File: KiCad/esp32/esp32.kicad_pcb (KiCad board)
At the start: 2 copper layers, 2 parts, among them U1 ESD7104MUTAG, U2 ESP32-S3-MINI-1-N8

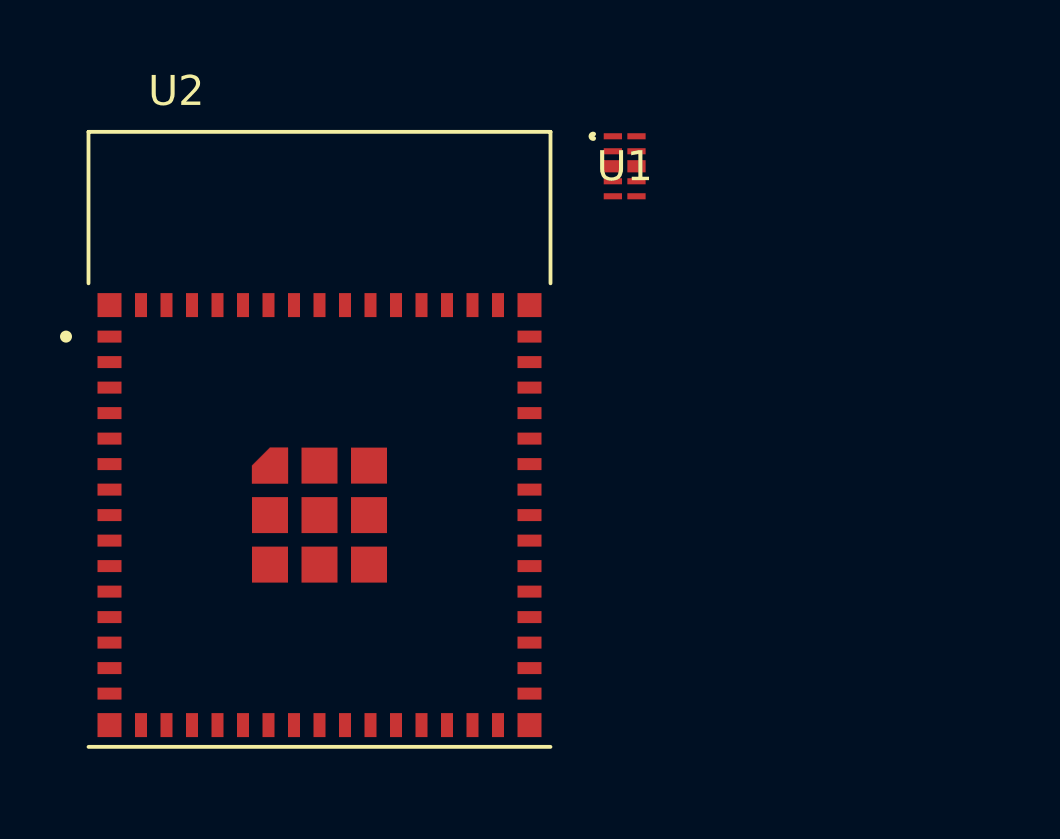
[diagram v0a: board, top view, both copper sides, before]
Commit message: restructed the path and file strcter
upaded schiemate and update pcb layout
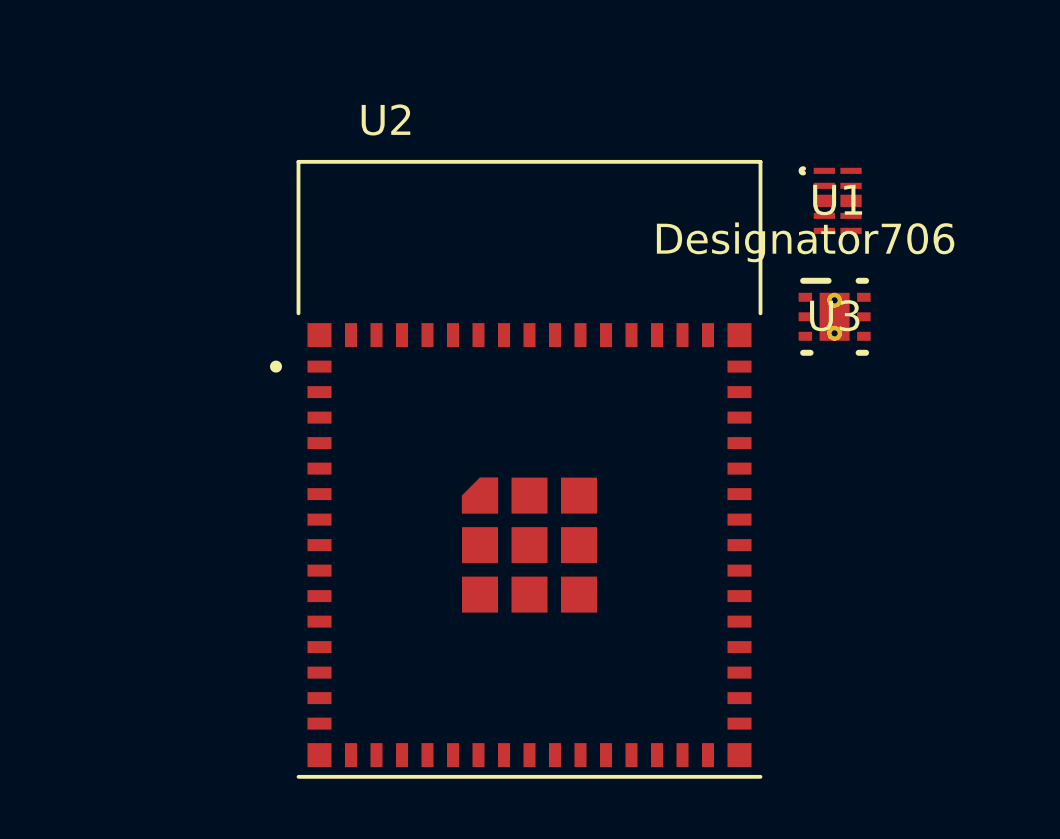
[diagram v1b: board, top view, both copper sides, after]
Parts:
- added U3: TLV75801PDRVR, Footprint:DRV0006A, F.Cu at (85.7, 92.4)
- U1: footprint footprints:UDFN10_ONS-L -> Footprint:UDFN10_ONS
- U2: footprint ESP32_S3_MINI_1_N8:XCVR_ESP32-S3-MINI-1-N8 -> Footprint:XCVR_ESP32-S3-MINI-1-N8
- moved U1 7.19 mm to (85.8, 88.5)
- moved U2 7.07 mm to (75.5, 100.0)

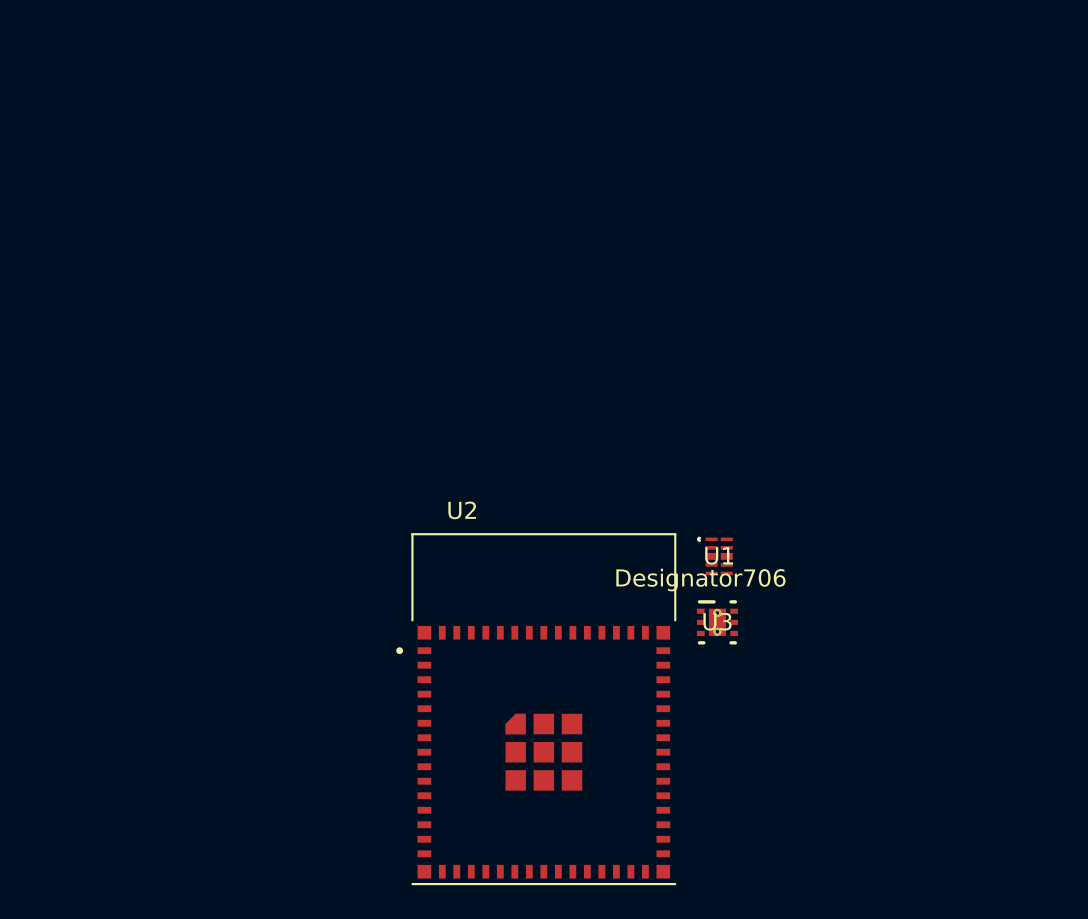
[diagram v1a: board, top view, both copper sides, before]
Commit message: layout started, footprints imported
pushed pcb
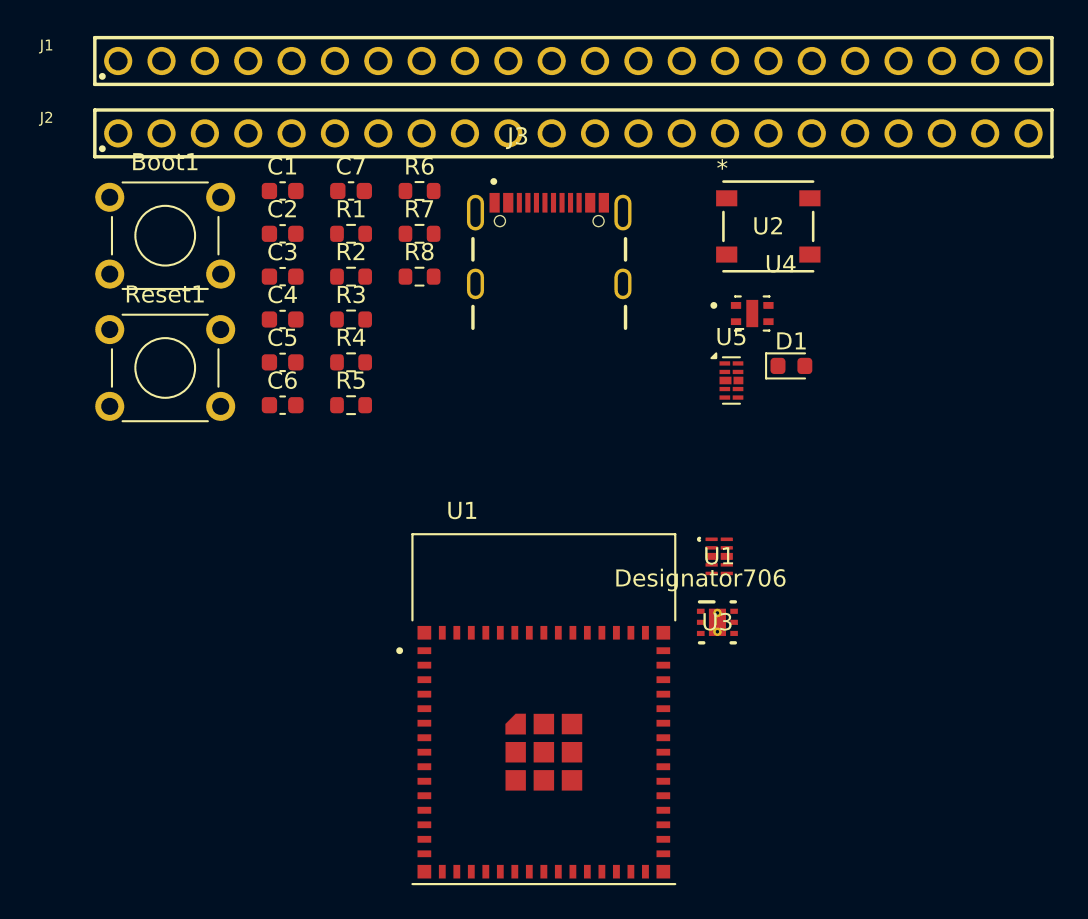
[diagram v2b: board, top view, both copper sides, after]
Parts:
- added Boot1: SW_Push_Dual, Button_Switch_THT:SW_TH_Tactile_Omron_B3F-100x, F.Cu at (50.1, 67.5)
- added C1: 0.1u, Capacitor_SMD:C_0603_1608Metric, F.Cu at (60.2, 67.1)
- added C2: 0.1u, Capacitor_SMD:C_0603_1608Metric, F.Cu at (60.2, 69.6)
- added C3: 0.1u, Capacitor_SMD:C_0603_1608Metric, F.Cu at (60.2, 72.1)
- added C4: 10u, Capacitor_SMD:C_0603_1608Metric, F.Cu at (60.2, 74.6)
- added C5: 10u, Capacitor_SMD:C_0603_1608Metric, F.Cu at (60.2, 77.2)
- added C6: 10u, Capacitor_SMD:C_0603_1608Metric, F.Cu at (60.2, 79.7)
- added C7: 0.1u, Capacitor_SMD:C_0603_1608Metric, F.Cu at (64.2, 67.1)
- added D1: LED, LED_SMD:LED_0603_1608Metric, F.Cu at (90.0, 77.4)
- added J1: 6130XX11121_61302211121, Footprint:61302211121, F.Cu at (77.2, 59.5)
- added J2: 6130XX11121_61302211121, Footprint:61302211121, F.Cu at (77.2, 63.7)
- added J3: USB4105-GF-A, Footprint:GCT_USB4105-GF-A, F.Cu at (75.8, 72.6)
- added R1: 10k, Resistor_SMD:R_0603_1608Metric, F.Cu at (64.2, 69.6)
- added R2: 10k, Resistor_SMD:R_0603_1608Metric, F.Cu at (64.2, 72.1)
- added R3: 10k, Resistor_SMD:R_0603_1608Metric, F.Cu at (64.2, 74.6)
- added R4: 5.1k, Resistor_SMD:R_0603_1608Metric, F.Cu at (64.2, 77.2)
- added R5: 5.1k, Resistor_SMD:R_0603_1608Metric, F.Cu at (64.2, 79.7)
- added R6: 1M, Resistor_SMD:R_0603_1608Metric, F.Cu at (68.2, 67.1)
- added R7: 200k, Resistor_SMD:R_0603_1608Metric, F.Cu at (68.2, 69.6)
- added R8: 5.1k, Resistor_SMD:R_0603_1608Metric, F.Cu at (68.2, 72.1)
- added Reset1: SW_Push_Dual, Button_Switch_THT:SW_TH_Tactile_Omron_B3F-100x, F.Cu at (50.1, 75.2)
- added U2: COM-16347, Footprint:COM-16347_SPK, F.Cu at (88.7, 69.2)
- added U4: ENS210-LQFM, Footprint:XDCR_ENS210-LQFM, F.Cu at (87.7, 74.3)
- added U5: D3V3XA4B10LP, Package_DFN_QFN:Diodes_UDFN-10_1.0x2.5mm_P0.5mm, F.Cu at (86.5, 78.2)
- renumbered U2 to U1
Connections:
- U1 pad 1: unconnected-(U2-GND-Pad1) -> GND
- U1 pad 10: unconnected-(U2-IO6-Pad10) -> /GPI06
- U1 pad 11: unconnected-(U2-IO7-Pad11) -> /GPI07
- U1 pad 12: unconnected-(U2-IO8-Pad12) -> /GPI08
- U1 pad 13: unconnected-(U2-IO9-Pad13) -> /GPI09
- U1 pad 14: unconnected-(U2-IO10-Pad14) -> /GPI010
- U1 pad 15: unconnected-(U2-IO11-Pad15) -> /GPI011
- U1 pad 16: unconnected-(U2-IO12-Pad16) -> /GPI012
- U1 pad 17: unconnected-(U2-IO13-Pad17) -> /GPI013
- U1 pad 18: unconnected-(U2-IO14-Pad18) -> /GPI014
- U1 pad 19: unconnected-(U2-IO15-Pad19) -> /GPI015
- U1 pad 2: unconnected-(U2-GND__1-Pad2) -> GND
- U1 pad 20: unconnected-(U2-IO16-Pad20) -> /GPI016
- U1 pad 21: unconnected-(U2-IO17-Pad21) -> /I2C_SCL
- U1 pad 22: unconnected-(U2-IO18-Pad22) -> /I2C_SDA
- U1 pad 23: unconnected-(U2-IO19-Pad23) -> /USB_N
- U1 pad 24: unconnected-(U2-IO20-Pad24) -> /USB_P
- U1 pad 25: unconnected-(U2-IO21-Pad25) -> /GPI021
- U1 pad 26: unconnected-(U2-IO26-Pad26) -> /GPI026
- U1 pad 27: unconnected-(U2-IO47-Pad27) -> /GPI047
- U1 pad 28: unconnected-(U2-IO33-Pad28) -> /GPI033
- U1 pad 29: unconnected-(U2-IO34-Pad29) -> /GPI034
- U1 pad 3: unconnected-(U2-3V3-Pad3) -> +3V3
- U1 pad 30: unconnected-(U2-IO48-Pad30) -> /GPI048
- U1 pad 31: unconnected-(U2-IO35-Pad31) -> /GPI035
- U1 pad 32: unconnected-(U2-IO36-Pad32) -> /GPI036
- U1 pad 33: unconnected-(U2-IO37-Pad33) -> /GPI037
- U1 pad 34: unconnected-(U2-IO38-Pad34) -> /GPI038
- U1 pad 35: unconnected-(U2-IO39-Pad35) -> /GPI039
- U1 pad 36: unconnected-(U2-IO40-Pad36) -> /GPI040
- U1 pad 37: unconnected-(U2-IO41-Pad37) -> /GPI041
- U1 pad 38: unconnected-(U2-IO42-Pad38) -> /GPI042
- U1 pad 39: unconnected-(U2-TXD0-Pad39) -> /TXD
- U1 pad 4: unconnected-(U2-IO0-Pad4) -> /GPI00
- U1 pad 40: unconnected-(U2-RXD0-Pad40) -> /RXD
- U1 pad 41: unconnected-(U2-IO45-Pad41) -> /GPI045
- U1 pad 42: unconnected-(U2-GND__2-Pad42) -> GND
- U1 pad 43: unconnected-(U2-GND__3-Pad43) -> GND
- U1 pad 44: unconnected-(U2-IO46-Pad44) -> /GPI046
- U1 pad 45: unconnected-(U2-EN-Pad45) -> /ESP32_EN
- U1 pad 46: unconnected-(U2-GND__4-Pad46) -> GND
- U1 pad 47: unconnected-(U2-GND__5-Pad47) -> GND
- U1 pad 48: unconnected-(U2-GND__6-Pad48) -> GND
- U1 pad 49: unconnected-(U2-GND__7-Pad49) -> GND
- U1 pad 5: unconnected-(U2-IO1-Pad5) -> /GPI01
- U1 pad 50: unconnected-(U2-GND__8-Pad50) -> GND
- U1 pad 51: unconnected-(U2-GND__9-Pad51) -> GND
- U1 pad 52: unconnected-(U2-GND__10-Pad52) -> GND
- U1 pad 53: unconnected-(U2-GND__11-Pad53) -> GND
- U1 pad 54: unconnected-(U2-GND__12-Pad54) -> GND
- U1 pad 55: unconnected-(U2-GND__13-Pad55) -> GND
- U1 pad 56: unconnected-(U2-GND__14-Pad56) -> GND
- U1 pad 57: unconnected-(U2-GND__15-Pad57) -> GND
- U1 pad 58: unconnected-(U2-GND__16-Pad58) -> GND
- U1 pad 59: unconnected-(U2-GND__17-Pad59) -> GND
- U1 pad 6: unconnected-(U2-IO2-Pad6) -> /GPI02
- U1 pad 60: unconnected-(U2-GND__18-Pad60) -> GND
- U1 pad 61: unconnected-(U2-GND__19-Pad61) -> GND
- U1 pad 61_1: unconnected-(U2-GND__20-Pad61_1) -> GND
- U1 pad 61_2: unconnected-(U2-GND__21-Pad61_2) -> GND
- U1 pad 61_3: unconnected-(U2-GND__22-Pad61_3) -> GND
- U1 pad 61_4: unconnected-(U2-GND__23-Pad61_4) -> GND
- U1 pad 61_5: unconnected-(U2-GND__24-Pad61_5) -> GND
- U1 pad 61_6: unconnected-(U2-GND__25-Pad61_6) -> GND
- U1 pad 61_7: unconnected-(U2-GND__26-Pad61_7) -> GND
- U1 pad 61_8: unconnected-(U2-GND__27-Pad61_8) -> GND
- U1 pad 62: unconnected-(U2-GND__28-Pad62) -> GND
- U1 pad 63: unconnected-(U2-GND__29-Pad63) -> GND
- U1 pad 64: unconnected-(U2-GND__30-Pad64) -> GND
- U1 pad 65: unconnected-(U2-GND__31-Pad65) -> GND
- U1 pad 7: unconnected-(U2-IO3-Pad7) -> /GPI03
- U1 pad 8: unconnected-(U2-IO4-Pad8) -> /GPI04
- U1 pad 9: unconnected-(U2-IO5-Pad9) -> /GPI05
- U3 pad 1: unconnected-(U3-OUT-Pad1) -> +3V3
- U3 pad 2: unconnected-(U3-FB-Pad2) -> Net-(U3-FB)
- U3 pad 3: unconnected-(U3-GND-Pad3) -> GND
- U3 pad 4: unconnected-(U3-EN-Pad4) -> +5V
- U3 pad 6: unconnected-(U3-IN-Pad6) -> +5V
- U3 pad 7: unconnected-(U3-PAD-Pad7) -> GND
